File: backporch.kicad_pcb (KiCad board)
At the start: 2 copper layers, 53.3 x 32.4 mm, 28 parts, among them J1 MD-90SM, J2 MD-80SM, J3 DB15_Female_HighDensity_Mount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, J4 35RAPC4BH3, U1 EL1883ISZ

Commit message: Add mounting holes
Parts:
- added H1: MountingHole, MountingHole:MountingHole_2.2mm_M2_ISO7380_Pad, F.Cu at (144.1, 104.1)
- added H2: MountingHole, MountingHole:MountingHole_2.2mm_M2_ISO7380_Pad, F.Cu at (144.1, 79.4)
- added H3: MountingHole, MountingHole:MountingHole_2.2mm_M2_ISO7380_Pad, F.Cu at (110.5, 91.4)
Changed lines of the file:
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@@
     (tracks 232)
     (zones 0)
-    (modules 28)
+    (modules 31)
     (nets 36)
   )
@@
     (add_net GND)
   )
+  (module MountingHole:MountingHole_2.2mm_M2_ISO7380_Pad (layer F.Cu)
+    (at 110.49 91.44)
+    (descr "Mounting Hole 2.2mm, M2, ISO7380")
+    (tags "mounting hole 2.2mm m2 iso7380")
+    (attr virtual)
+    (fp_text reference H3 (at 0 -2.75) (layer F.SilkS) hide
+      (effects (font (size 1 1) (thickness 0.15)))
+    )
+    (fp_text value MountingHole (at 0 2.75) (layer F.Fab)
+      (effects (font (size 1 1) (thickness 0.15)))
+    )
+    (fp_text user %R (at 0.3 0) (layer F.Fab)
+      (effects (font (size 1 1) (thickness 0.15)))
+    )
+    (fp_circle (center 0 0) (end 1.75 0) (layer Cmts.User) (width 0.15))
+    (fp_circle (center 0 0) (end 2 0) (layer F.CrtYd) (width 0.05))
+    (pad 1 thru_hole circle (at 0 0) (size 3.5 3.5) (drill 2.2) (layers *.Cu *.Mask))
+  )
+  (module MountingHole:MountingHole_2.2mm_M2_ISO7380_Pad (layer F.Cu)
+    (at 144.145 79.375)
+    (descr "Mounting Hole 2.2mm, M2, ISO7380")
+    (tags "mounting hole 2.2mm m2 iso7380")
+    (attr virtual)
+    (fp_text reference H2 (at 0 -2.75) (layer F.SilkS) hide
+      (effects (font (size 1 1) (thickness 0.15)))
+    )
+    (fp_text value MountingHole (at 0 2.75) (layer F.Fab)
+      (effects (font (size 1 1) (thickness 0.15)))
+    )
+    (fp_circle (center 0 0) (end 2 0) (layer F.CrtYd) (width 0.05))
+    (fp_circle (center 0 0) (end 1.75 0) (layer Cmts.User) (width 0.15))
+    (fp_text user %R (at 0.3 0) (layer F.Fab)
+      (effects (font (size 1 1) (thickness 0.15)))
+    )
+    (pad 1 thru_hole circle (at 0 0) (size 3.5 3.5) (drill 2.2) (layers *.Cu *.Mask))
+  )
+  (module MountingHole:MountingHole_2.2mm_M2_ISO7380_Pad (layer F.Cu)
+    (at 144.145 104.14)
+    (descr "Mounting Hole 2.2mm, M2, ISO7380")
+    (tags "mounting hole 2.2mm m2 iso7380")
+    (attr virtual)
+    (fp_text reference H1 (at 0 -2.75) (layer F.SilkS) hide
+      (effects (font (size 1 1) (thickness 0.15)))
+    )
+    (fp_text value MountingHole (at 0 2.75) (layer F.Fab)
+      (effects (font (size 1 1) (thickness 0.15)))
+    )
+    (fp_text user %R (at 0.3 0) (layer F.Fab)
+      (effects (font (size 1 1) (thickness 0.15)))
+    )
+    (fp_circle (center 0 0) (end 1.75 0) (layer Cmts.User) (width 0.15))
+    (fp_circle (center 0 0) (end 2 0) (layer F.CrtYd) (width 0.05))
+    (pad 1 thru_hole circle (at 0 0) (size 3.5 3.5) (drill 2.2) (layers *.Cu *.Mask))
+  )
   (module Jumper:SolderJumper-3_P1.3mm_Open_Pad1.0x1.5mm (layer B.Cu)

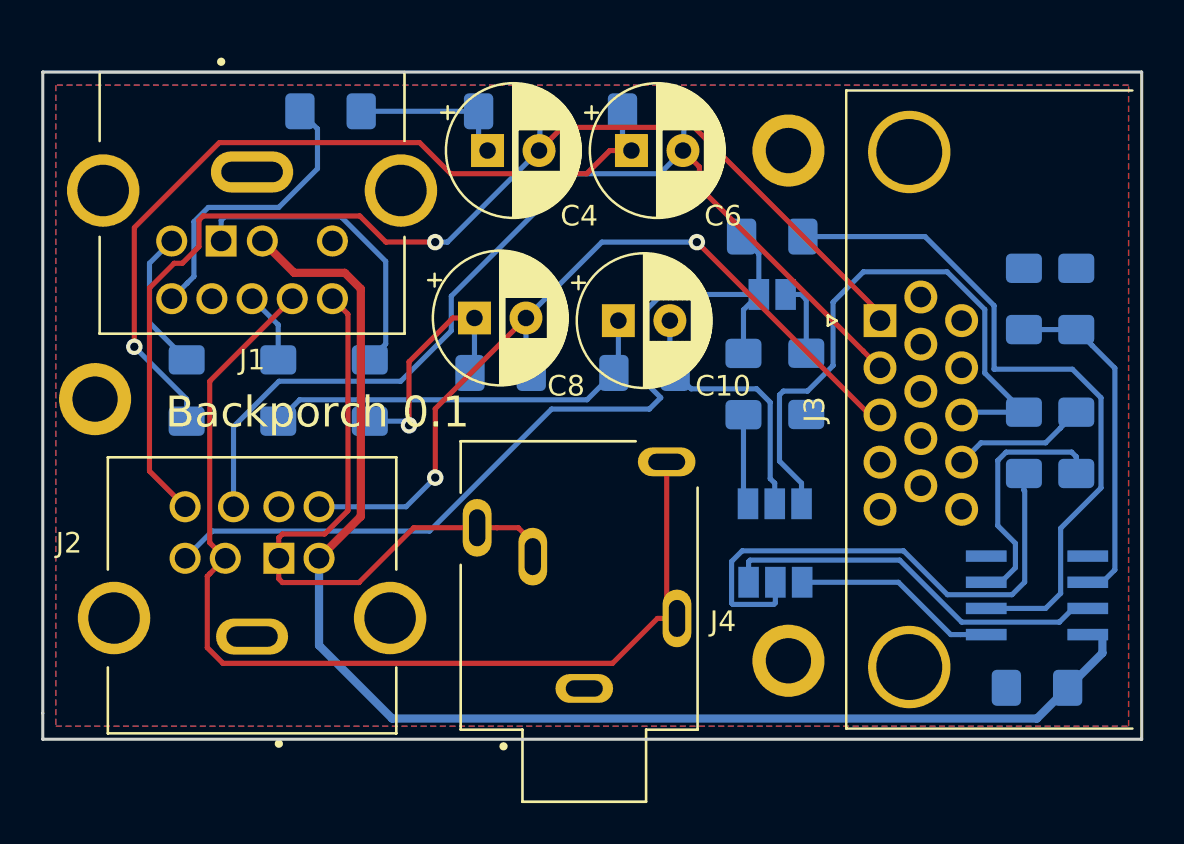
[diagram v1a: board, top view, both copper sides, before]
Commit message: Backporch 0.2: Swap pin 3 and 5 on mini-DIN 8
For some reason, CUI devices labeling of their pins for their mini-DIN 8
is different from everybody else's and also different from their other
mini DIN connectors.

This fixes a major issue where +5V and sync were swapped on the
mini-DIN 8 connector.
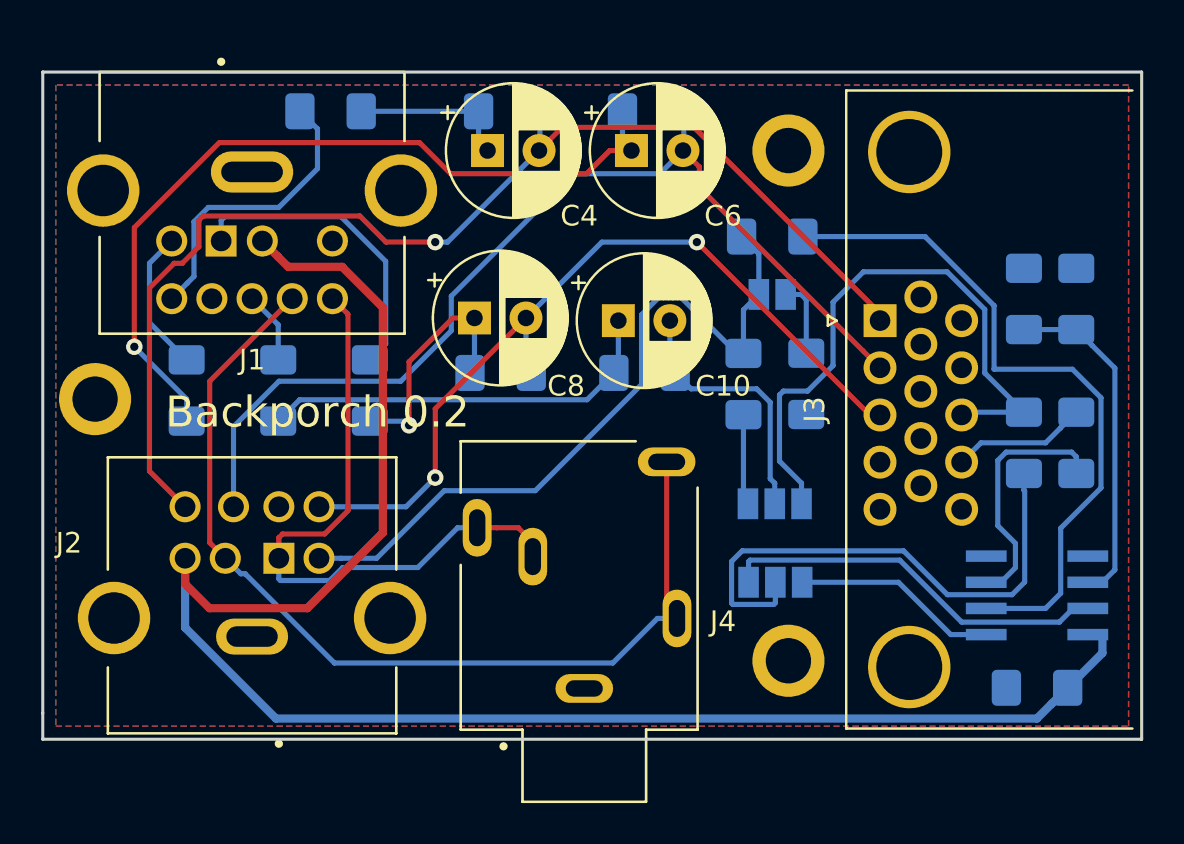
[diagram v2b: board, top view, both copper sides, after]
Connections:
- J2 pad 3: CSYNC_75 -> +5V
- J2 pad 5: +5V -> CSYNC_75
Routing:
- net +5V: track 66.2 -> 83.5 mm
- net CSYNC_75: track 43.0 -> 35.3 mm
- net AUD_LEFT: track 51.1 -> 47.3 mm
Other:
- board text added: "Backporch 0.2"
- board text removed: "Backporch 0.1"
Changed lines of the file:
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@@
     (thickness 1.6)
     (drawings 6)
-    (tracks 232)
+    (tracks 238)
     (zones 0)
     (modules 31)
@@
       (net 10 BLUE_75))
     (pad 5 thru_hole circle (at 3.25 -1.8) (size 1.508 1.508) (drill 1) (layers *.Cu *.Mask)
+      (net 5 CSYNC_75))
+    (pad 3 thru_hole circle (at -3.25 -1.8) (size 1.508 1.508) (drill 1) (layers *.Cu *.Mask)
       (net 2 +5V))
-    (pad 3 thru_hole circle (at -3.25 -1.8) (size 1.508 1.508) (drill 1) (layers *.Cu *.Mask)
-      (net 5 CSYNC_75))
     (pad 8 thru_hole circle (at -3.25 -4.3) (size 1.508 1.508) (drill 1) (layers *.Cu *.Mask)
       (net 6 RED_75))
@@
       (net 2 +5V))
   )
-  (gr_text "Backporch 0.1" (at 121.285 92.075) (layer F.SilkS)
+  (gr_text "Backporch 0.2" (at 121.285 92.075) (layer F.SilkS)
     (effects (font (size 1.5 1.5) (thickness 0.3)))
   )
@@
   (segment (start 159.385 103.765184) (end 159.385 102.87) (width 0.4) (layer B.Cu) (net 2) (status 20))
   (segment (start 118.61 84.32) (end 118.61 83.765) (width 0.4) (layer B.Cu) (net 2) (status 30))
-  (segment (start 123.389009 97.135991) (end 121.36 99.165) (width 0.4) (layer F.Cu) (net 2) (status 20))
-  (segment (start 123.389009 86.088087) (end 123.389009 97.135991) (width 0.4) (layer F.Cu) (net 2))
-  (segment (start 122.611921 85.310999) (end 123.389009 86.088087) (width 0.4) (layer F.Cu) (net 2))
-  (segment (start 120.155999 85.310999) (end 122.611921 85.310999) (width 0.4) (layer F.Cu) (net 2))
-  (segment (start 118.61 83.765) (end 120.155999 85.310999) (width 0.4) (layer F.Cu) (net 2) (status 10))
-  (segment (start 121.36 103.395443) (end 121.36 100.231317) (width 0.4) (layer B.Cu) (net 2))
-  (segment (start 156.205183 106.945001) (end 124.909558 106.945001) (width 0.4) (layer B.Cu) (net 2))
-  (segment (start 121.36 100.231317) (end 121.36 99.165) (width 0.4) (layer B.Cu) (net 2))
-  (segment (start 124.909558 106.945001) (end 121.36 103.395443) (width 0.4) (layer B.Cu) (net 2))
-  (segment (start 157.6975 105.452684) (end 156.205183 106.945001) (width 0.4) (layer B.Cu) (net 2))
+  (segment (start 114.86 99.165) (end 114.86 100.405) (width 0.4) (layer F.Cu) (net 2))
+  (segment (start 120.790932 101.58999) (end 124.46 97.920922) (width 0.4) (layer F.Cu) (net 2))
+  (segment (start 114.86 100.405) (end 116.04499 101.58999) (width 0.4) (layer F.Cu) (net 2))
+  (segment (start 116.04499 101.58999) (end 120.790932 101.58999) (width 0.4) (layer F.Cu) (net 2))
+  (segment (start 119.363999 84.518999) (end 118.61 83.765) (width 0.4) (layer F.Cu) (net 2))
+  (segment (start 119.864001 85.019001) (end 119.363999 84.518999) (width 0.4) (layer F.Cu) (net 2))
+  (segment (start 122.484001 85.019001) (end 119.864001 85.019001) (width 0.4) (layer F.Cu) (net 2))
+  (segment (start 124.46 86.995) (end 122.484001 85.019001) (width 0.4) (layer F.Cu) (net 2))
+  (segment (start 124.46 97.920922) (end 124.46 86.995) (width 0.4) (layer F.Cu) (net 2))
+  (segment (start 156.926153 106.224031) (end 157.6975 105.452684) (width 0.4) (layer B.Cu) (net 2))
+  (segment (start 156.205183 106.945001) (end 156.926153 106.224031) (width 0.4) (layer B.Cu) (net 2))
+  (segment (start 119.270444 106.945001) (end 156.205183 106.945001) (width 0.4) (layer B.Cu) (net 2))
+  (segment (start 114.86 102.534557) (end 119.270444 106.945001) (width 0.4) (layer B.Cu) (net 2))
+  (segment (start 114.86 99.165) (end 114.86 102.534557) (width 0.4) (layer B.Cu) (net 2))
   (segment (start 155.575 88.065) (end 158.115 88.065) (width 0.25) (layer B.Cu) (net 3))
   (segment (start 158.886347 88.836347) (end 158.115 88.065) (width 0.25) (layer B.Cu) (net 3))
@@
   (segment (start 142.708595 84.388944) (end 141.871095 83.551444) (width 0.25) (layer B.Cu) (net 5) (status 20))
   (segment (start 142.708595 86.36) (end 142.708595 84.388944) (width 0.25) (layer B.Cu) (net 5) (status 10))
-  (segment (start 126.726416 97.844001) (end 116.180999 97.844001) (width 0.25) (layer B.Cu) (net 5))
-  (segment (start 132.647917 91.9225) (end 126.726416 97.844001) (width 0.25) (layer B.Cu) (net 5))
-  (segment (start 142.708595 86.36) (end 137.994998 86.36) (width 0.25) (layer B.Cu) (net 5) (status 10))
-  (segment (start 137.994998 86.36) (end 137.264999 87.089999) (width 0.25) (layer B.Cu) (net 5))
-  (segment (start 137.39433 91.9225) (end 132.647917 91.9225) (width 0.25) (layer B.Cu) (net 5))
-  (segment (start 137.264999 87.089999) (end 137.264999 90.688189) (width 0.25) (layer B.Cu) (net 5))
-  (segment (start 137.264999 90.688189) (end 137.94682 91.37001) (width 0.25) (layer B.Cu) (net 5))
-  (segment (start 116.180999 97.844001) (end 114.86 99.165) (width 0.25) (layer B.Cu) (net 5) (status 20))
-  (segment (start 137.94682 91.37001) (end 137.39433 91.9225) (width 0.25) (layer B.Cu) (net 5))
+  (segment (start 124.158002 99.165) (end 122.426317 99.165) (width 0.25) (layer B.Cu) (net 5))
+  (segment (start 127.438002 95.885) (end 124.158002 99.165) (width 0.25) (layer B.Cu) (net 5))
+  (segment (start 131.85819 95.885) (end 127.438002 95.885) (width 0.25) (layer B.Cu) (net 5))
+  (segment (start 137.015001 90.728189) (end 131.85819 95.885) (width 0.25) (layer B.Cu) (net 5))
+  (segment (start 137.015001 87.339997) (end 137.015001 90.728189) (width 0.25) (layer B.Cu) (net 5))
+  (segment (start 122.426317 99.165) (end 121.36 99.165) (width 0.25) (layer B.Cu) (net 5))
+  (segment (start 137.849999 86.504999) (end 137.015001 87.339997) (width 0.25) (layer B.Cu) (net 5))
+  (segment (start 138.930001 86.504999) (end 137.849999 86.504999) (width 0.25) (layer B.Cu) (net 5))
+  (segment (start 141.647446 89.222444) (end 138.930001 86.504999) (width 0.25) (layer B.Cu) (net 5))
+  (segment (start 141.961595 89.222444) (end 141.647446 89.222444) (width 0.25) (layer B.Cu) (net 5))
   (via (at 127 83.82) (size 0.8) (drill 0.4) (layers F.Cu B.Cu) (net 6))
   (segment (start 148.59 87.63) (end 148.310002 87.63) (width 0.25) (layer F.Cu) (net 6) (status 30))
@@
   (segment (start 122.763999 87.318999) (end 122.763999 96.857923) (width 0.25) (layer F.Cu) (net 18))
   (segment (start 122.01 86.565) (end 122.763999 87.318999) (width 0.25) (layer F.Cu) (net 18) (status 10))
-  (segment (start 125.959158 97.685) (end 129.035 97.685) (width 0.25) (layer F.Cu) (net 18) (status 20))
-  (segment (start 123.300157 100.344001) (end 125.959158 97.685) (width 0.25) (layer F.Cu) (net 18))
-  (segment (start 119.585001 100.344001) (end 123.300157 100.344001) (width 0.25) (layer F.Cu) (net 18))
-  (segment (start 119.41 100.169) (end 119.585001 100.344001) (width 0.25) (layer F.Cu) (net 18))
-  (segment (start 119.41 99.165) (end 119.41 100.169) (width 0.25) (layer F.Cu) (net 18) (status 10))
   (segment (start 129.985 97.685) (end 129.035 97.685) (width 0.25) (layer F.Cu) (net 18))
   (segment (start 131.035 97.685) (end 129.985 97.685) (width 0.25) (layer F.Cu) (net 18))
   (segment (start 131.735 98.385) (end 131.035 97.685) (width 0.25) (layer F.Cu) (net 18))
   (segment (start 131.735 99.085) (end 131.735 98.385) (width 0.25) (layer F.Cu) (net 18))
+  (segment (start 128.085 97.685) (end 129.035 97.685) (width 0.25) (layer B.Cu) (net 18))
+  (segment (start 126.15499 99.61501) (end 128.085 97.685) (width 0.25) (layer B.Cu) (net 18))
+  (segment (start 122.506912 99.61501) (end 126.15499 99.61501) (width 0.25) (layer B.Cu) (net 18))
+  (segment (start 121.877921 100.244001) (end 122.506912 99.61501) (width 0.25) (layer B.Cu) (net 18))
+  (segment (start 119.485001 100.244001) (end 121.877921 100.244001) (width 0.25) (layer B.Cu) (net 18))
+  (segment (start 119.41 100.169) (end 119.485001 100.244001) (width 0.25) (layer B.Cu) (net 18))
+  (segment (start 119.41 99.165) (end 119.41 100.169) (width 0.25) (layer B.Cu) (net 18))
   (segment (start 138.235 101.585) (end 138.735 102.085) (width 0.25) (layer F.Cu) (net 20) (status 30))
   (segment (start 138.235 94.485) (end 138.235 101.585) (width 0.25) (layer F.Cu) (net 20) (status 30))
   (segment (start 116.056001 90.568999) (end 120.06 86.565) (width 0.25) (layer F.Cu) (net 20) (status 20))
+  (segment (start 116.81 99.165) (end 116.056001 98.411001) (width 0.25) (layer F.Cu) (net 20) (status 10))
   (segment (start 116.056001 98.411001) (end 116.056001 90.568999) (width 0.25) (layer F.Cu) (net 20))
-  (segment (start 116.81 99.165) (end 116.056001 98.411001) (width 0.25) (layer F.Cu) (net 20) (status 10))
-  (segment (start 115.93499 100.04001) (end 116.056001 99.918999) (width 0.25) (layer F.Cu) (net 20))
-  (segment (start 115.93499 103.503481) (end 115.93499 100.04001) (width 0.25) (layer F.Cu) (net 20))
-  (segment (start 116.696519 104.26501) (end 115.93499 103.503481) (width 0.25) (layer F.Cu) (net 20))
-  (segment (start 135.60499 104.26501) (end 116.696519 104.26501) (width 0.25) (layer F.Cu) (net 20))
-  (segment (start 137.785 102.085) (end 135.60499 104.26501) (width 0.25) (layer F.Cu) (net 20))
-  (segment (start 116.056001 99.918999) (end 116.81 99.165) (width 0.25) (layer F.Cu) (net 20))
-  (segment (start 138.735 102.085) (end 137.785 102.085) (width 0.25) (layer F.Cu) (net 20))
+  (segment (start 117.563999 99.918999) (end 116.81 99.165) (width 0.25) (layer B.Cu) (net 20))
+  (segment (start 117.77749 99.918999) (end 117.563999 99.918999) (width 0.25) (layer B.Cu) (net 20))
+  (segment (start 122.106492 104.248001) (end 117.77749 99.918999) (width 0.25) (layer B.Cu) (net 20))
+  (segment (start 135.621999 104.248001) (end 122.106492 104.248001) (width 0.25) (layer B.Cu) (net 20))
+  (segment (start 137.785 102.085) (end 135.621999 104.248001) (width 0.25) (layer B.Cu) (net 20))
+  (segment (start 138.735 102.085) (end 137.785 102.085) (width 0.25) (layer B.Cu) (net 20))
   (segment (start 119.38 87.835) (end 119.38 89.535) (width 0.25) (layer B.Cu) (net 21) (status 20))
   (segment (start 118.11 86.565) (end 119.38 87.835) (width 0.25) (layer B.Cu) (net 21) (status 10))

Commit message: Update DE-15/VGA connector footprint
KiCad's DE-15 footprint is not correct for right angle connectors,
making it difficult to fit standard connectors.

Use VGA_CONN footprint from the OSSC project at
https://github.com/marqs85/ossc_pcb instead as a workaround.
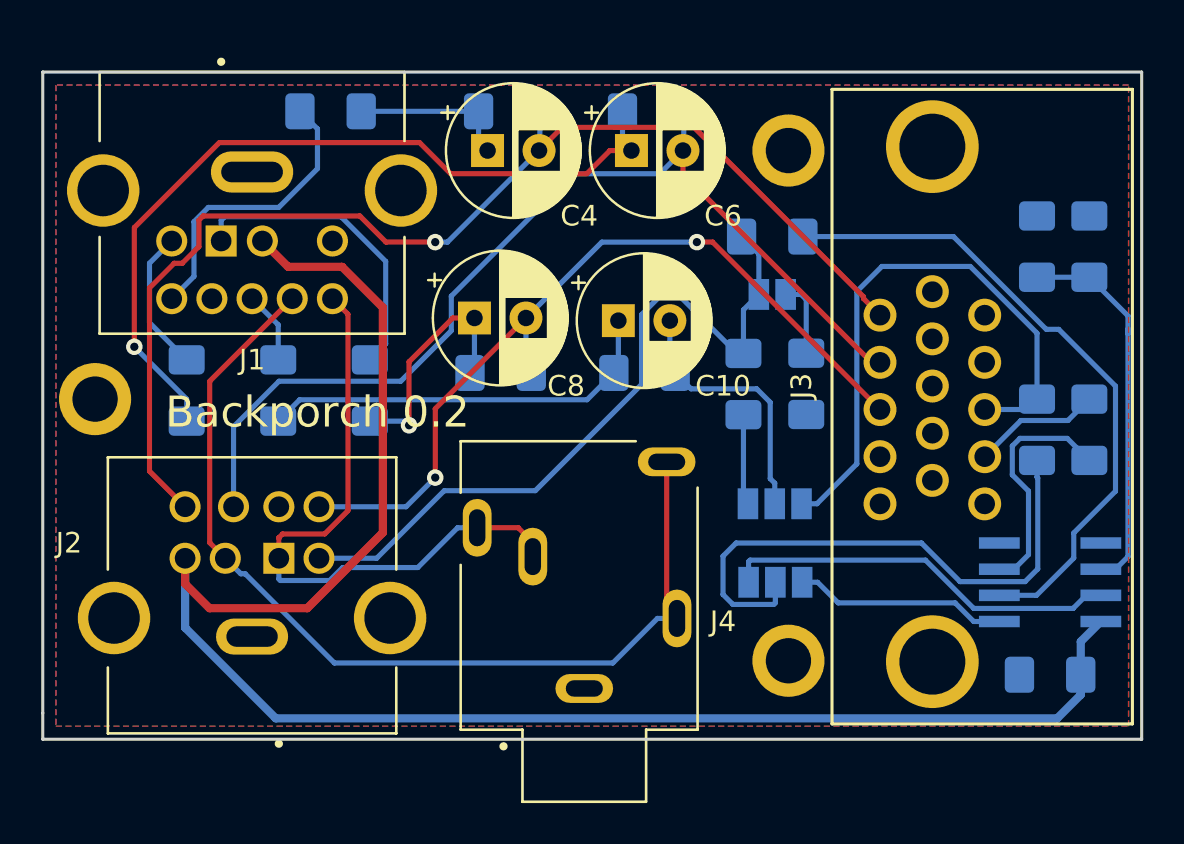
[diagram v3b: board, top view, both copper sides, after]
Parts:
- J3: footprint Connector_Dsub:DSUB-15-HD_Female_Horizontal_P2.29x1.98mm_EdgePinOffset8.35mm_Housed_MountingHolesOffset10.89mm -> VGA-from-OSSC:VGA_CONN
- moved J3 4.07 mm to (151.1, 90.8)
- moved R2 2.62 mm to (156.2, 84.0)
- moved C2 2.62 mm to (158.8, 84.0)
- moved R8 0.90 mm to (156.2, 92.9)
- moved C1 0.90 mm to (156.8, 104.8)
- moved R9 0.90 mm to (158.8, 92.9)
- moved U1 0.90 mm to (156.8, 100.3)
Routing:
- net Net-(C2-Pad1): track 16.5 -> 18.7 mm
- net Net-(JP3-Pad2): track 26.1 -> 27.5 mm
- net Net-(C3-Pad1): track 33.7 -> 32.3 mm
- net HSYNC_75: track 29.6 -> 28.4 mm
- net +5V: track 83.5 -> 84.6 mm
- net RED_75: track 58.5 -> 58.0 mm
- net Net-(R9-Pad2): track 12.2 -> 11.6 mm

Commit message: PCB: add GitHub URL to silkscreen
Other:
- board text added: "github.com/semi-simple/backporch"
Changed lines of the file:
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@@
   (general
     (thickness 1.6)
-    (drawings 6)
+    (drawings 7)
     (tracks 227)
     (zones 0)
@@
       (net 2 +5V))
   )
+  (gr_text github.com/semi-simple/backporch (at 120.65 106.045) (layer B.SilkS)
+    (effects (font (size 0.8 0.8) (thickness 0.16)) (justify mirror))
+  )
   (gr_text "Backporch 0.2" (at 121.285 92.075) (layer F.SilkS)
